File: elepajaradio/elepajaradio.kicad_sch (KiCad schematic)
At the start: 18 parts

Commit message: kicad update
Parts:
- removed AE?: Antenna, symbol Device:Antenna
- removed C? (x3): C, symbol Device:C
- removed LS?: Speaker, symbol Device:Speaker
- removed R?: R_US, symbol Device:R_US
- removed SW?: SW_SPDT, symbol Switch:SW_SPDT
- removed U?: Opamp_Dual, symbol Device:Opamp_Dual
- removed Y?: Crystal, symbol Device:Crystal
- added AE1: Antenna, symbol Device:Antenna
- added C3, C6: C_Variable, symbol Device:C_Variable
- added C4, C5: C, symbol Device:C
- added L1, L2: L, symbol Device:L
- added Q1, Q2: 2N2219, Package_TO_SOT_THT:TO-39-3, symbol Transistor_BJT:2N2219
- added R1, R3: R_US, symbol Device:R_US
- gave numbers to parts that had none: 9
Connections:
- net GND: now also Q2.1 (E), R1.2, R3.2; no longer R2.1, U3.2 (-)
- net PWR: now also C3.1, C6.1, L1.1, L2.1
- net at R2.2, U3.1: now also Q1.2 (B)
- new net: C3.2, C4.1, L1.2, Q1.3 (C)
- new net: R1.1, R2.1, U3.2 (-)
- new net: C4.2, C5.1, Q1.1 (E), R3.1
- new net: C5.2, Q2.2 (B)
- new net: AE1.1 (A), C6.2, L2.2, Q2.3 (C)
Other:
- moved on the sheet: C1, C2, MK1, R2, SW1, U1, U2, U3A, Y1

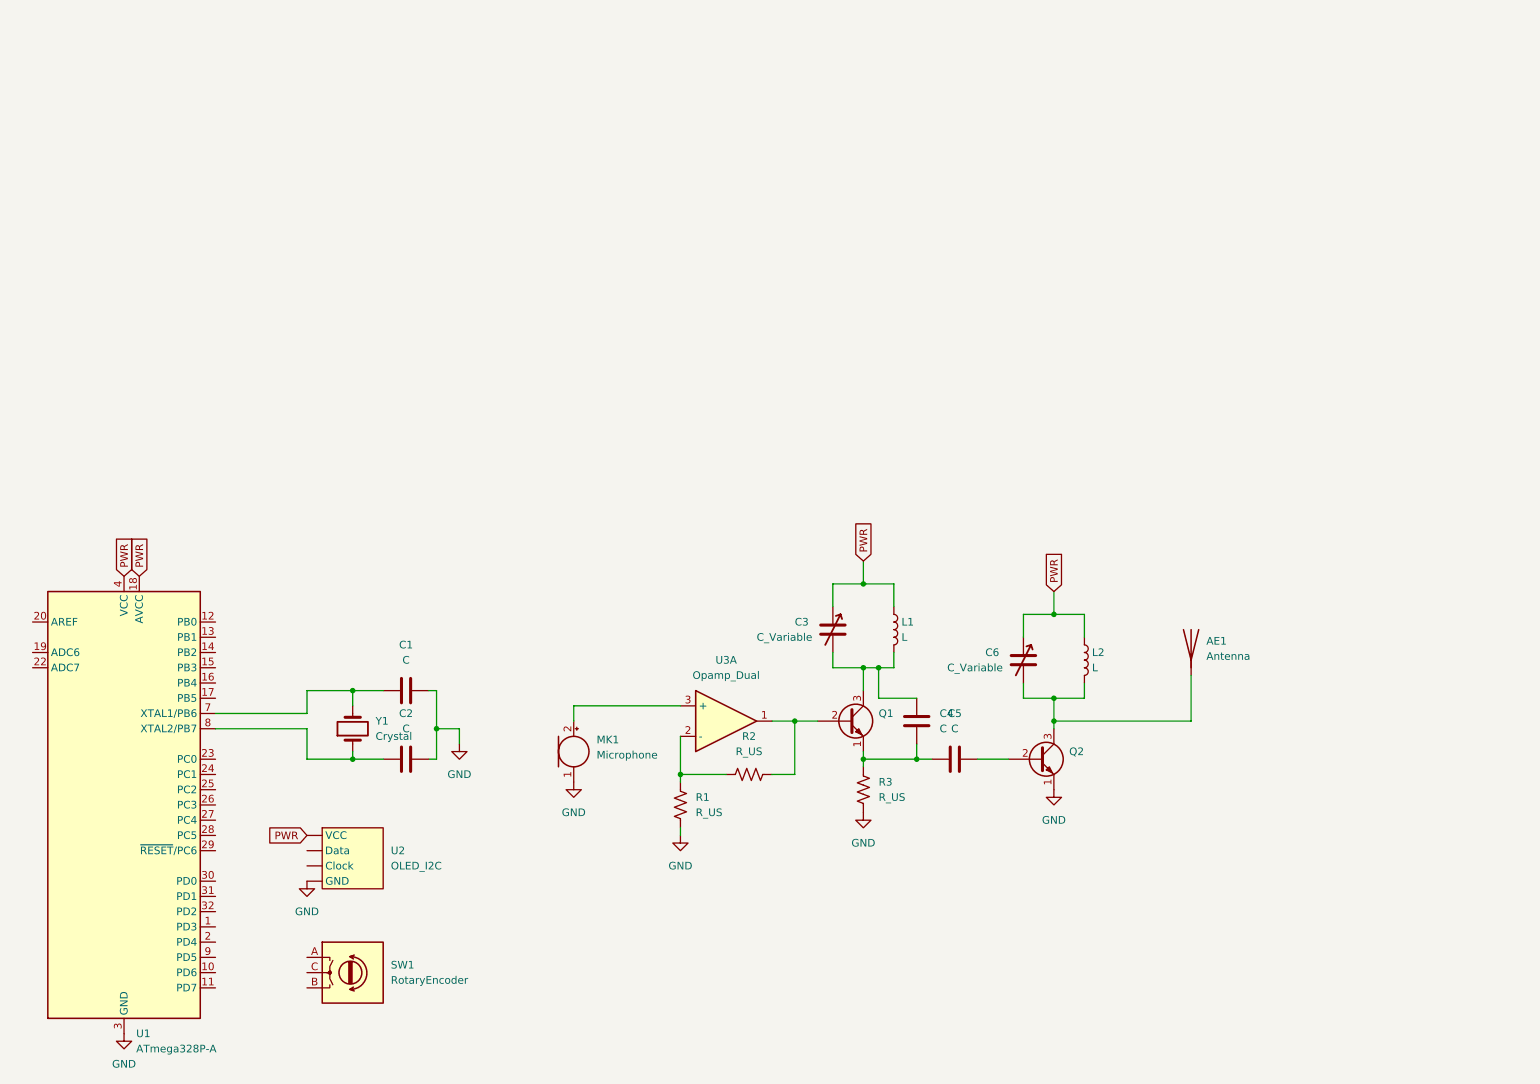
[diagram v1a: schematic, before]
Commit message: adding doc file and spice simulation file
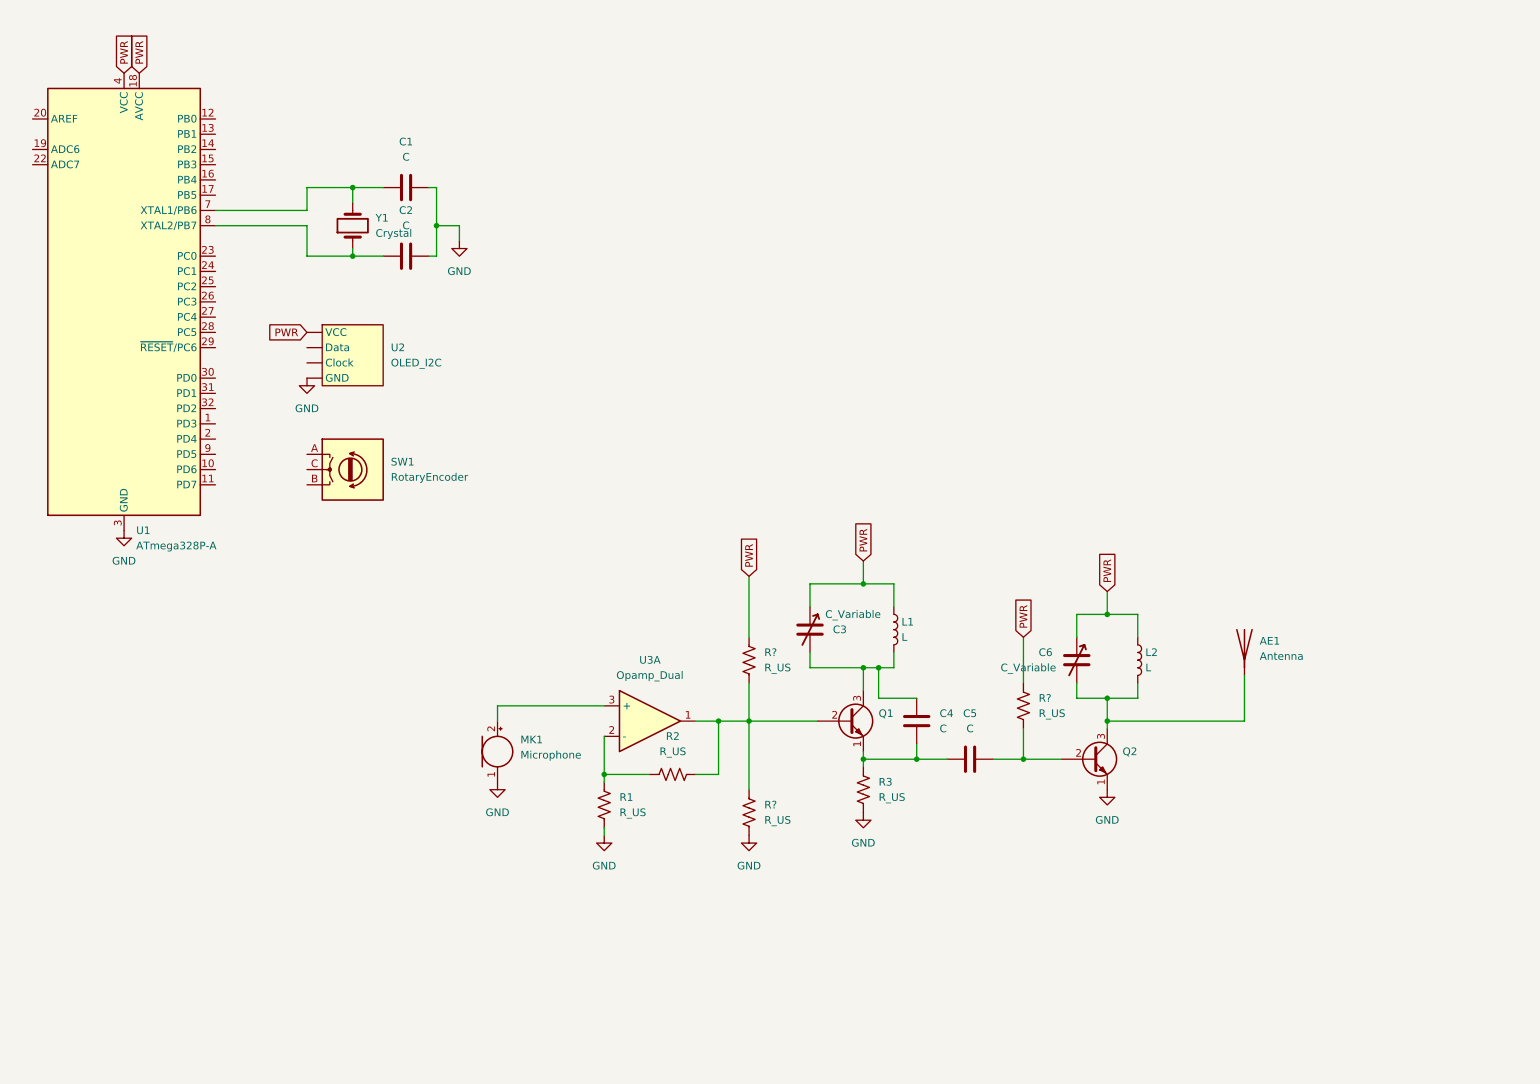
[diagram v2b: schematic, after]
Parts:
- added R? (x3): R_US, symbol Device:R_US
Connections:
- net GND: now also R?.2
- net PWR: now also R?.1, R?.1
- net at Q1.2 (B), R2.2, U3.1: now also R?.1, R?.2
- net at C5.2, Q2.2 (B): now also R?.2
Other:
- moved on the sheet: AE1, C1, C2, C3, C5, C6, L2, MK1, Q2, R1, R2, SW1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

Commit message: new circuit added
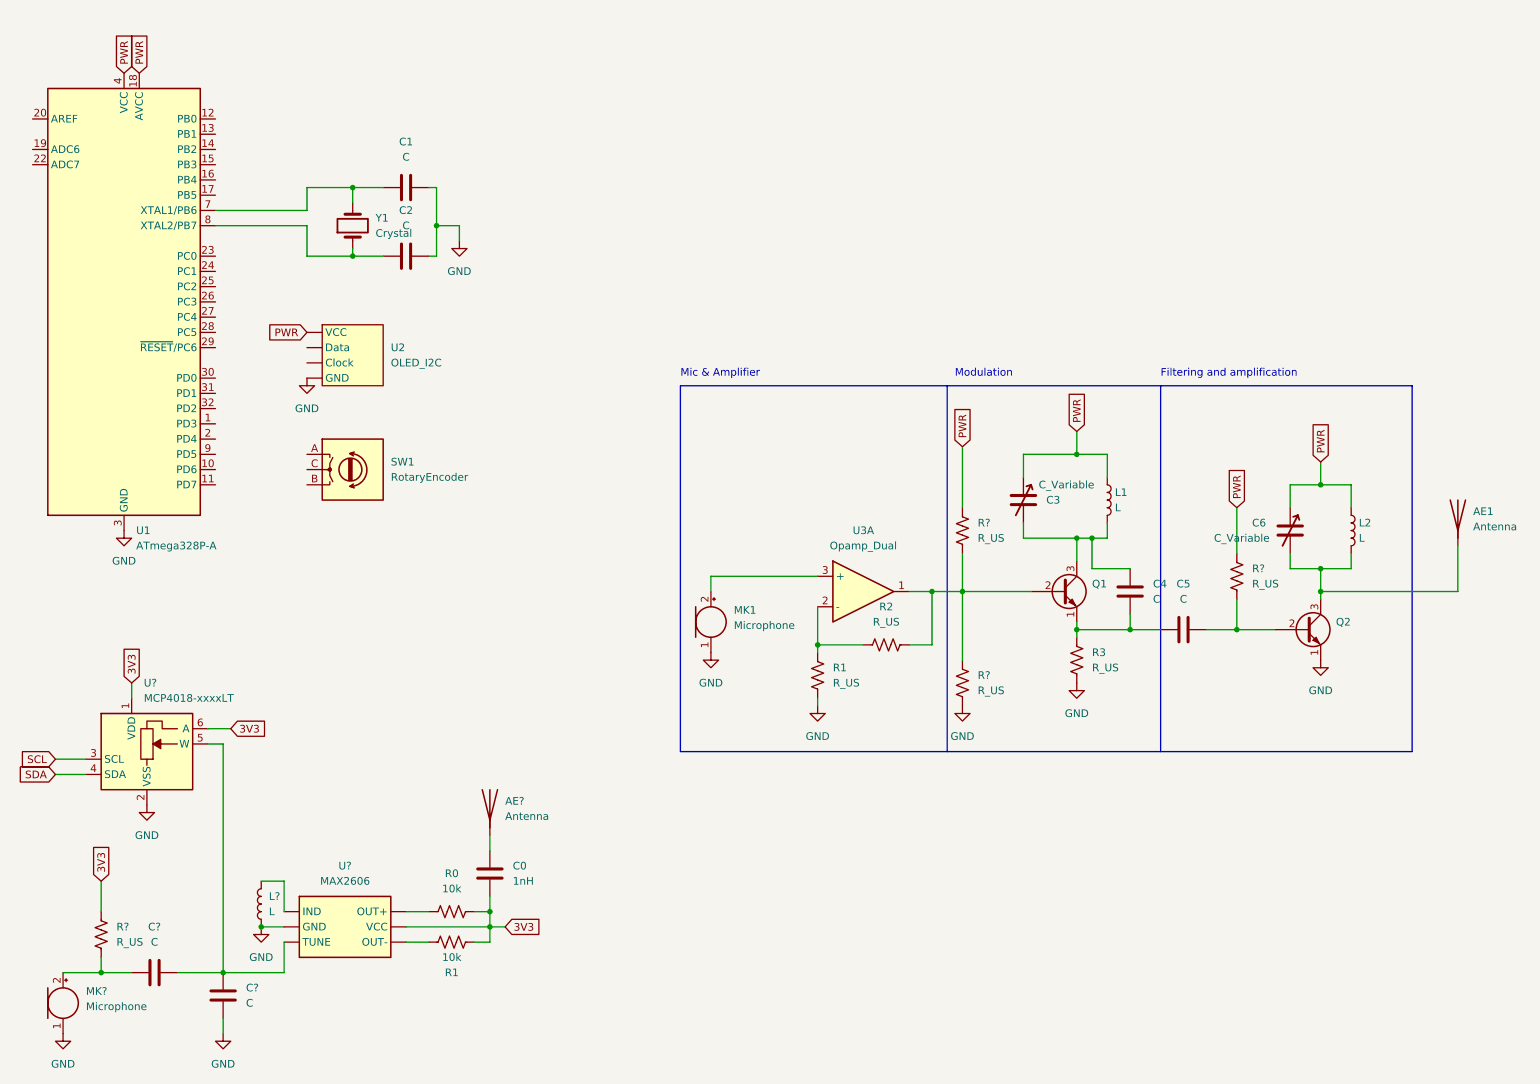
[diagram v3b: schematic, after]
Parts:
- added AE?: Antenna, symbol Device:Antenna
- added C0: 1nH, symbol Device:C
- added C? (x2): C, symbol Device:C
- added L?: L, symbol Device:L
- added MK?: Microphone, symbol Device:Microphone
- added R0, R1: 10k, Resistor_SMD:R_0201_0603Metric_Pad0.64x0.40mm_HandSolder, symbol Device:R_US
- added R?: R_US, symbol Device:R_US
- added U?: MAX2606, Package_TO_SOT_SMD:SOT-23-6, symbol max2606:MAX2606
- added U?: MCP4018-xxxxLT, Package_TO_SOT_SMD:SOT-363_SC-70-6, symbol Potentiometer_Digital:MCP4018-xxxxLT
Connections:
- net GND: now also C?.2, L?.1, MK?.1 (-), U?. (VCC), U?.2 (VSS)
- new net: AE?.1 (A), C0.1
- new net: C?.1, MK?.2 (+), R?.1
- new net: C?.1, C?.2, U?. (VCC), U?.5 (W)
- new net: R0.1, U?. (VCC)
- new net: R1.1, U?. (VCC)
- new net: L?.2, U?. (VCC)
- new net 3V3: C0.2, R0.2, R1.2, R?.2, U?. (VCC), U?.1 (VDD), U?.6 (A)
- new net SCL: U?.3 (SCL)
- new net SDA: U?.4 (SDA)
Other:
- note added: "Filtering and amplification"
- note added: "Mic & Amplifier"
- note added: "Modulation"
- moved on the sheet: AE1, C3, C4, C5, C6, L1, L2, MK1, Q1, Q2, R1, R2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

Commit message: MCU
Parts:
- removed AE1: Antenna, symbol Device:Antenna
- removed C3, C6: C_Variable, symbol Device:C_Variable
- removed L1, L2: L, symbol Device:L
- removed MK1: Microphone, symbol Device:Microphone
- removed Q1, Q2: 2N2219, Package_TO_SOT_THT:TO-39-3, symbol Transistor_BJT:2N2219
- removed R1, R2, R3, R? (x3): R_US, symbol Device:R_US
- removed U1: ATmega328P-A, Package_QFP:TQFP-32_7x7mm_P0.8mm, symbol MCU_Microchip_ATmega:ATmega328P-A
- removed U3: Opamp_Dual, symbol Device:Opamp_Dual
- added C3: 1uF, symbol Device:C
- added J1: SPI, symbol Connector:Conn_01x04_Pin
- added J2: UART, symbol Connector:Conn_01x02_Pin
- added J3: vdd_gnd, symbol Connector:Conn_01x02_Pin
- added J4: reset, symbol Connector:Conn_01x01_Pin
- added R2, R3: 10k, symbol Device:R
- added SW2, SW3: SW_Push, symbol Switch:SW_Push
- added U3: ATmega328PB-A, Package_QFP:TQFP-32_7x7mm_P0.8mm, symbol MCU_Microchip_ATmega:ATmega328PB-A
- added U4: AP2204K-ADJ, Package_TO_SOT_SMD:SOT-23-5, symbol Regulator_Linear:AP2204K-ADJ
- C4: value C -> 2.2uF
- C5: value C -> 100pF
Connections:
- net PWR is gone; now on net SDA0: U2. (VCC)
- net SDA is gone; now on net SDA0: U?.4 (SDA)
- net 3V3: no longer U?.1 (VDD), U?.6 (A)
- net GND: now also C4.2, C5.2, C3.2, J3.2 (Pin_2), R2.2, R3.2, U3.21 (GND), U3.5 (GND), U4.2 (GND)
- net SDA0: now reaches U2. (VCC)
- net SDA0: now also U3.27 (PC4)
- net +3.3V: now reaches C4.1
- net +3.3V: now also U2. (VCC), U?.1 (VDD), U?.6 (A), U4.5 (VOUT)
- net at C2.1, Y1.1: now also U3.8 (XTAL2/PB7)
- net at C1.1, Y1.2: now also U3.7 (XTAL1/PB6)
- net at C5.1: now also U4.4 (ADJ); no longer C4.2
- net VDD: now reaches SW1.A
- net VDD: now also C3.1, J3.1 (Pin_1), SW2.2, SW3.2, U3.4 (VCC), U4.1 (VIN), U4.3 (EN)
- net at SW1.B: now also U3.2 (PD4)
- net at SW1.C: now also U3.1 (PD3)
- net SCL renamed SCL0
- net SCL0: now also U2. (VCC), U3.28 (PC5)
- new net: J1.1 (Pin_1), U3.17 (PB5)
- new net: J1.2 (Pin_2), U3.16 (PB4)
- new net: J1.3 (Pin_3), U3.15 (PB3)
- new net: J1.4 (Pin_4), U3.14 (PB2)
- new net: J2.1 (Pin_1), U3.30 (PD0)
- new net: J2.2 (Pin_2), U3.31 (PD1)
- new net: J4.1 (Pin_1), U3.29 (~{RESET}/PC6)
- new net: R2.1, SW3.1, U3.13 (PB1)
- new net: R3.1, SW2.1, U3.12 (PB0)
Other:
- note removed: "Filtering and amplification"
- note removed: "Mic & Amplifier"
- note removed: "Modulation"
- moved on the sheet: AE?, C0, C1, C2, C?, L?, MK?, R0, R1, R?, SW1, U2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

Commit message: update
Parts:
- removed C0: 1nH, symbol Device:C
- removed C?: C, symbol Device:C
- removed R0: 10k, Resistor_SMD:R_0201_0603Metric_Pad0.64x0.40mm_HandSolder, symbol Device:R_US
- removed R2, R3: 10k, symbol Device:R
- removed U?: MAX2606, Package_TO_SOT_SMD:SOT-23-6, symbol max2606:MAX2606
- added C6, C7: C, Capacitor_SMD:C_0603_1608Metric, symbol Device:C
- added R2, R3, R4: R_US, Resistor_SMD:R_0603_1608Metric, symbol Device:R_US
- added U1: MAX2606, symbol max2606:MAX2606
- C1, C2, C?: footprint (none) -> Capacitor_SMD:C_0603_1608Metric
- C3: value 1uF -> C; footprint (none) -> Capacitor_SMD:C_0603_1608Metric
- C4: value 2.2uF -> C; footprint (none) -> Capacitor_SMD:C_0603_1608Metric
- C5: value 100pF -> C; footprint (none) -> Capacitor_SMD:C_0603_1608Metric
- J1, U2: footprint (none) -> Connector_PinHeader_2.54mm:PinHeader_1x04_P2.54mm_Vertical
- J2, J3, MK?: footprint (none) -> Connector_PinHeader_2.54mm:PinHeader_1x02_P2.54mm_Vertical
- J4: footprint (none) -> Connector_PinHeader_2.54mm:PinHeader_1x01_P2.54mm_Vertical
- L?: footprint (none) -> Inductor_SMD:L_0603_1608Metric
- R1: value 10k -> R_US; footprint Resistor_SMD:R_0201_0603Metric_Pad0.64x0.40mm_HandSolder -> Resistor_SMD:R_0603_1608Metric
- R?: footprint (none) -> Resistor_SMD:R_0603_1608Metric
- SW1: footprint (none) -> Connector_PinHeader_2.54mm:PinHeader_1x03_P2.54mm_Vertical
- Y1: footprint (none) -> Oscillator:Oscillator_SMD_Abracon_ASDMB-4Pin_2.5x2.0mm
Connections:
- net 3V3: now also R1.1, C7.2, R4.1, U1.5 (VCC); no longer R1.2
- net GND: now also R2.1, R3.1, U1.2 (GND)
- net at U3.8 (XTAL2/PB7), Y1.1: now also C1.1; no longer C2.1
- net at U3.7 (XTAL1/PB6), Y1.2: now also C2.1; no longer C1.1
- net at AE?.1 (A): now also C7.1
- net at MK?.2 (+), R?.1: now also C6.1
- net at C?.1, U?.5 (W): now also C6.2, U1.3 (TUNE)
- net at SW3.1, U3.13 (PB1): now also R2.2
- net at SW2.1, U3.12 (PB0): now also R3.2
- net at L?.2: now also U1.1 (IND)
- new net: R1.2, U1.4 (OUT-)
- new net: R4.2, U1.6 (OUT+)
